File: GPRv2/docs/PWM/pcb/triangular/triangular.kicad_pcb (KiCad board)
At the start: 2 copper layers, 27 parts, among them J1 Pote 100k (Bourns 3590), J2 12 V, J3 Salida, U1 TLC2274, U2 TLC2274

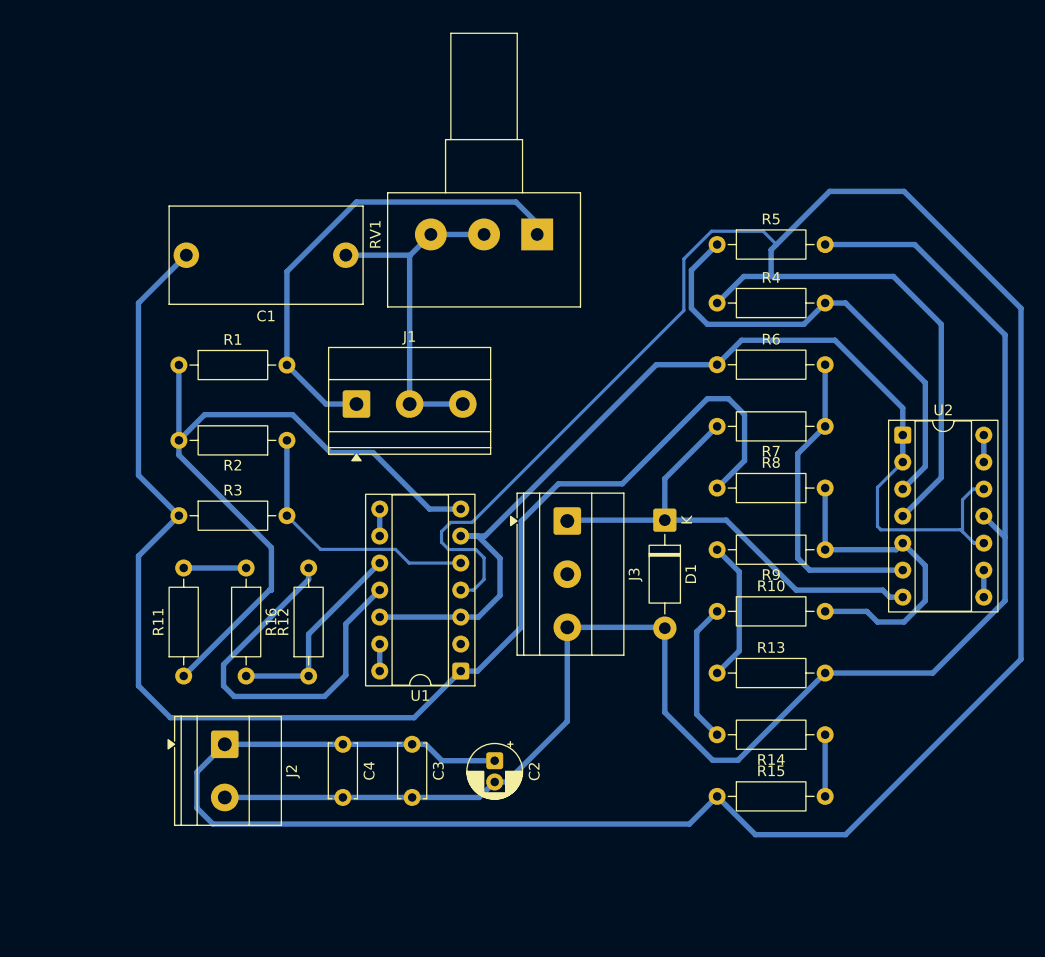
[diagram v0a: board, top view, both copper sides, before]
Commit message: GPRv2: PCB del generador de triangular terminado
- Esquematico: 2 TLC2274 repartidos por funcion (U1: integrador, Schmitt y
  sync; U2: 6 V y restador); las 3 unidades que sobran van como seguidor con
  la + a GND, asi mid no cruza la placa.
- SW1: llave palanca SPDT (LP-SW-213CI) de encendido en los 12 V, con LED
  rojo 5x5 (D2 + R17 2k2, ~4,7 mA). Se descarto el PULS-2I-RET: medido, su
  comun es un extremo de cada fila, no la pata del medio.
- JP1: puente de cable a 22,5 mm en la salida, antes de D1.
- triangular.pretty + fp-lib-table: huellas propias (llave a 4 mm con pads
  angostos, puente de 22,5 mm y el pulsador 8x8 por si se vuelve a usar).
- simular_kicad.py: detecta solo los operacionales que sobran, toma sq/tri/
  mid por etiqueta, simula la llave cerrada, el puente y el LED.
- PCB ruteado a una capa.

Co-Authored-By: Claude Opus 5.5 <noreply@anthropic.com>
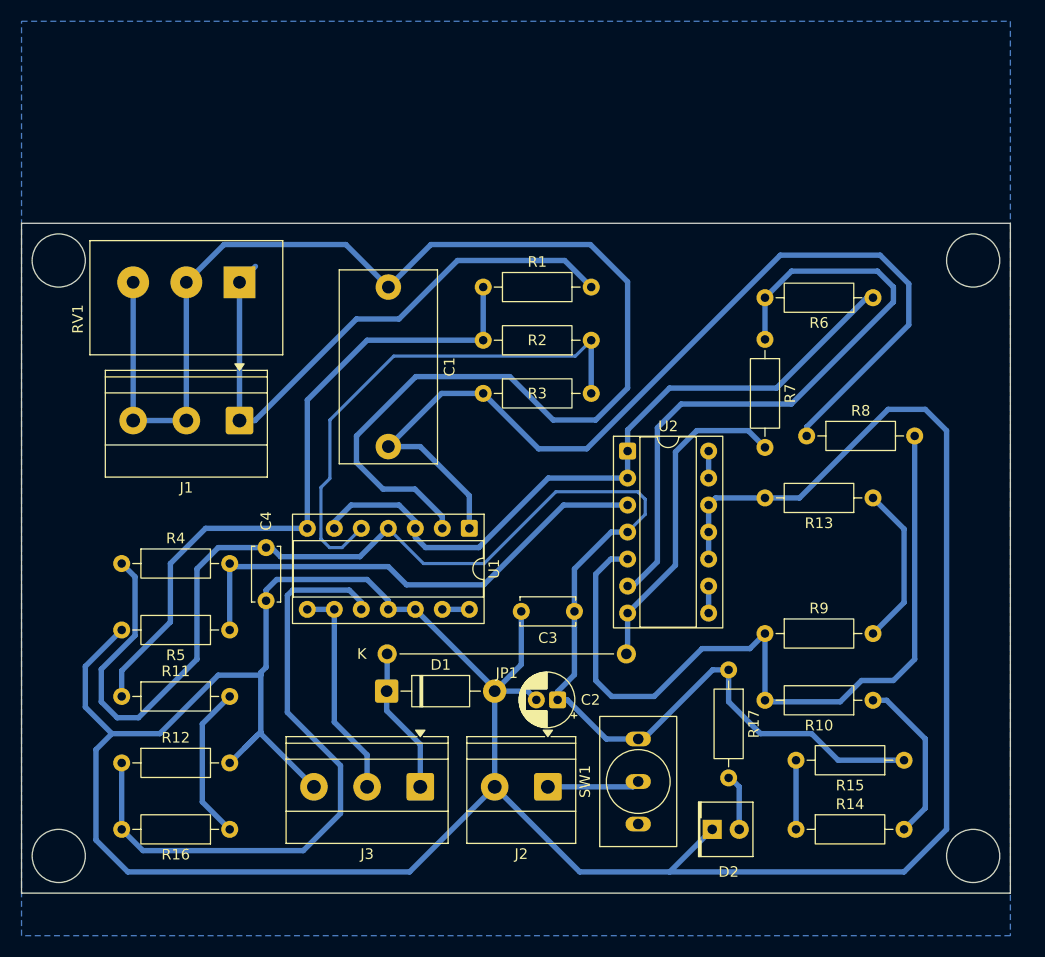
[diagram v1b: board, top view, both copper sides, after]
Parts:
- added D2: LED rojo 5x5, LED_THT:LED_Rectangular_W5.0mm_H5.0mm, F.Cu at (102.5, 98.0)
- added JP1: Puente, triangular:Puente_Cable_P22.5mm, F.Cu at (94.4, 81.5)
- added R17: 2k2, Resistor_THT:R_Axial_DIN0207_L6.3mm_D2.5mm_P10.16mm_Horizontal, F.Cu at (104.0, 83.0)
- added SW1: LP-SW-213CI, triangular:SW_Palanca_SPDT_P4mm, F.Cu at (95.5, 93.5)
- moved R4 61.1 mm to (46.9, 73.0)
- moved R5 58.4 mm to (57.1, 79.2), turned to 180 degrees
- moved R3 30.8 mm to (80.9, 57.0)
- moved D1 30.7 mm to (71.8, 85.0), turned to 0 degrees
- moved J2 30.6 mm to (87.0, 94.0), turned to 180 degrees
- moved R2 30.1 mm to (91.1, 52.0)
- moved R1 29.5 mm to (80.9, 47.0)
- moved J3 28.6 mm to (75.0, 94.0), turned to 180 degrees
- moved RV1 28.4 mm to (58.0, 46.5)
- moved U2 25.9 mm to (94.5, 62.4)
- moved R16 24.6 mm to (57.1, 98.0), turned to 180 degrees
- moved R13 22.0 mm to (117.6, 66.8), turned to 180 degrees
- moved C4 19.9 mm to (60.5, 71.5)
- moved C3 19.7 mm to (89.5, 77.5), turned to 180 degrees
- moved R12 19.4 mm to (46.9, 91.8), turned to 0 degrees
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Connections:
- J2 pad 1: +12V -> Net-(J2-Pin_1)
- R7 pad 2: /salida -> Net-(JP1-A)
- U1 pad 12: /mid -> GND
- U2 pad 10: /mid -> GND
- U2 pad 12: /mid -> GND
- U2 pad 7: /salida -> Net-(JP1-A)
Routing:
- net +12V: track 286.8 -> 149.4 mm
- net /inv: track 32.8 -> 134.7 mm
- net GND: track 186.0 -> 279.4 mm
- net Net-(U2B-+): track 30.3 -> 75.7 mm
- net Net-(U1C-+): track 19.3 -> 60.0 mm
- net /tri: track 130.6 -> 92.7 mm
- net /mid: track 100.7 -> 66.8 mm
- net Net-(U2B--): track 29.6 -> 62.5 mm
- net /salida: track 45.4 -> 13.8 mm
- net Net-(JP1-A): track 0.00 -> 30.8 mm
- net Net-(U1B-+): track 25.3 -> 49.1 mm
- net /sync: track 2.54 -> 20.5 mm
- net /pote: track 45.0 -> 55.5 mm
- net Net-(R11-Pad2): track 5.88 -> 14.6 mm
- net Net-(J2-Pin_1): track 0.00 -> 8.71 mm
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- added copper zone on B.Cu, net GND
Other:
- board outline added: 93 x 63 mm

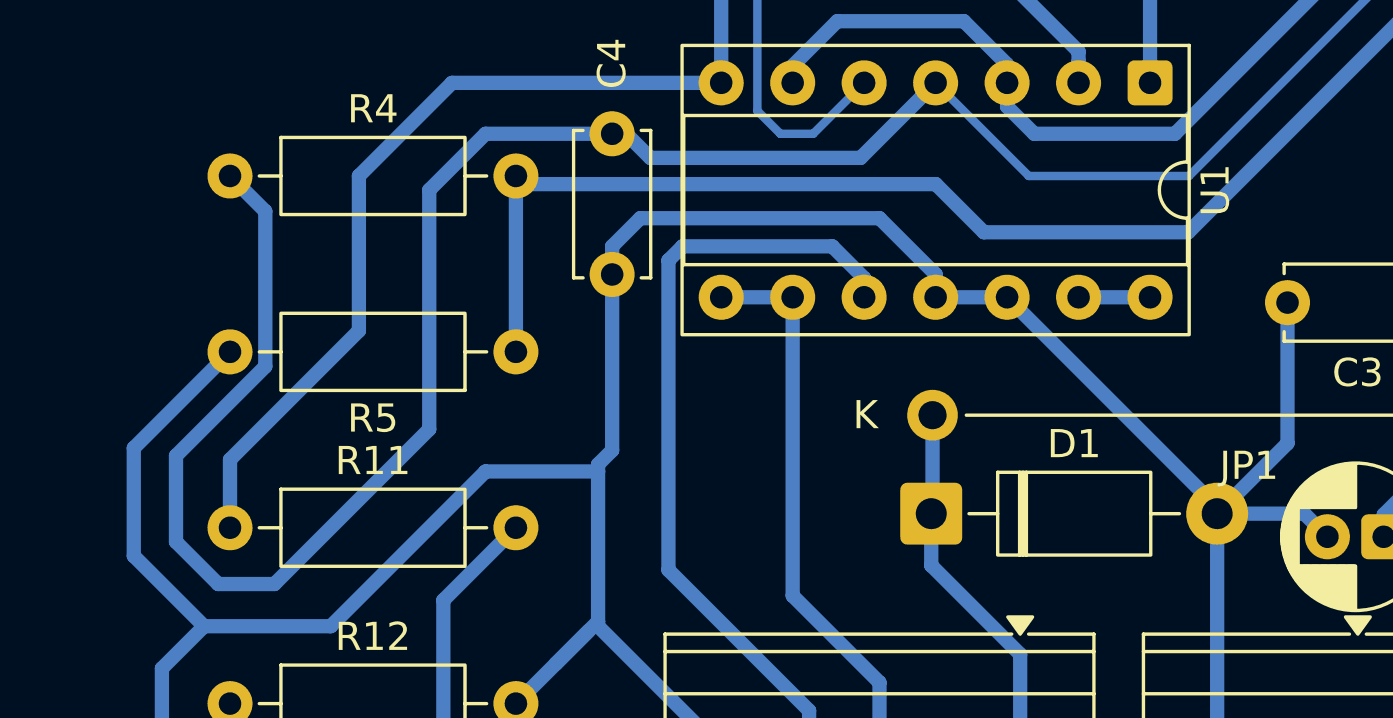
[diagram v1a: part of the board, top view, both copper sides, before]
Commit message: GPRv2: PCB de la triangular, version final revisada
- Pista de +12V separada del pad de GND de R5 (estaba a 0,2 mm) y zona GND
  recalculada: el relleno viejo tocaba esa pista (corto de 12 V a masa).
- Zona GND con alivios termicos y ancho minimo de 0,5 mm.
- Revisado: DRC con paridad contra el esquematico sin errores, redes de los
  pads iguales al circuito, y los 19 elementos de triangular3.asc con su par
  exacto en la placa.

Co-Authored-By: Claude Opus 5.5 <noreply@anthropic.com>
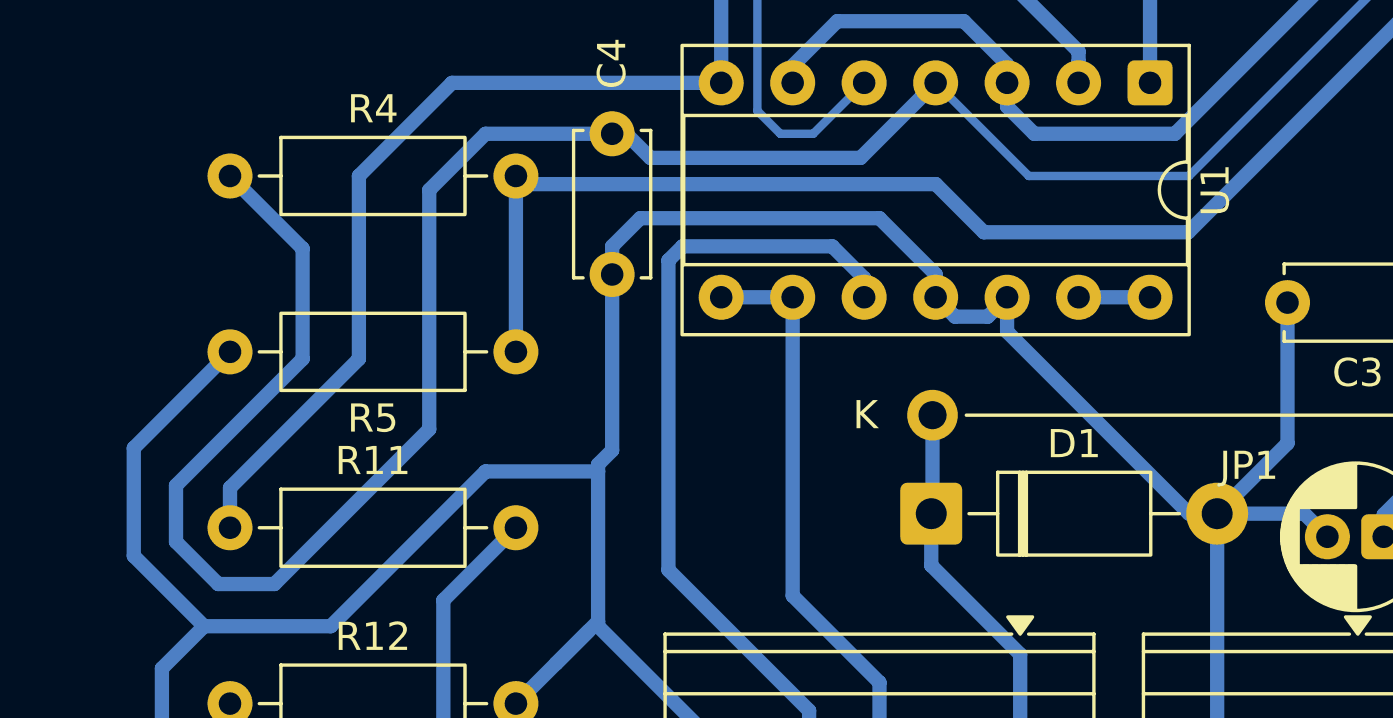
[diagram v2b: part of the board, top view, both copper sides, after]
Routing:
- net GND: track 279.4 -> 280.6 mm
- net +12V: track 149.4 -> 150.5 mm
